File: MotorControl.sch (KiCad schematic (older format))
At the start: 6 parts, among them U3 74LVC125, X1 16MHz

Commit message: Add missing files from the TMC2130 branch.
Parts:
- C3, C81, C82, C90: footprint Capacitor_SMD:C_0603_1608Metric -> PrntrBoardV1:C_0603_1608Metric
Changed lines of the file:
@@
 F 0 "C3" H 8215 4346 50  0000 L CNN
 F 1 "0.1uF" H 8215 4255 50  0000 L CNN
-F 2 "Capacitor_SMD:C_0603_1608Metric" H 8138 4150 50  0001 C CNN
+F 2 "PrntrBoardV1:C_0603_1608Metric" H 8138 4150 50  0001 C CNN
 F 3 "~" H 8100 4300 50  0001 C CNN
 	1    8100 4300
@@
 F 0 "C90" H 9550 4350 50  0000 L CNN
 F 1 "0.1uF" H 9550 4250 50  0000 L CNN
-F 2 "Capacitor_SMD:C_0603_1608Metric" H 9488 4300 50  0001 C CNN
+F 2 "PrntrBoardV1:C_0603_1608Metric" H 9488 4300 50  0001 C CNN
 F 3 "~" H 9450 4450 50  0001 C CNN
 	1    9450 4450
@@
 F 0 "C81" H 7865 4346 50  0000 L CNN
 F 1 "1000pF" H 7800 4200 50  0000 L CNN
-F 2 "Capacitor_SMD:C_0603_1608Metric" H 7788 4150 50  0001 C CNN
+F 2 "PrntrBoardV1:C_0603_1608Metric" H 7788 4150 50  0001 C CNN
 F 3 "~" H 7750 4300 50  0001 C CNN
 	1    7750 4300
@@
 F 0 "C82" H 9250 4350 50  0000 L CNN
 F 1 "1000pF" H 9150 4150 50  0000 L CNN
-F 2 "Capacitor_SMD:C_0603_1608Metric" H 9238 4300 50  0001 C CNN
+F 2 "PrntrBoardV1:C_0603_1608Metric" H 9238 4300 50  0001 C CNN
 F 3 "~" H 9200 4450 50  0001 C CNN
 	1    9200 4450

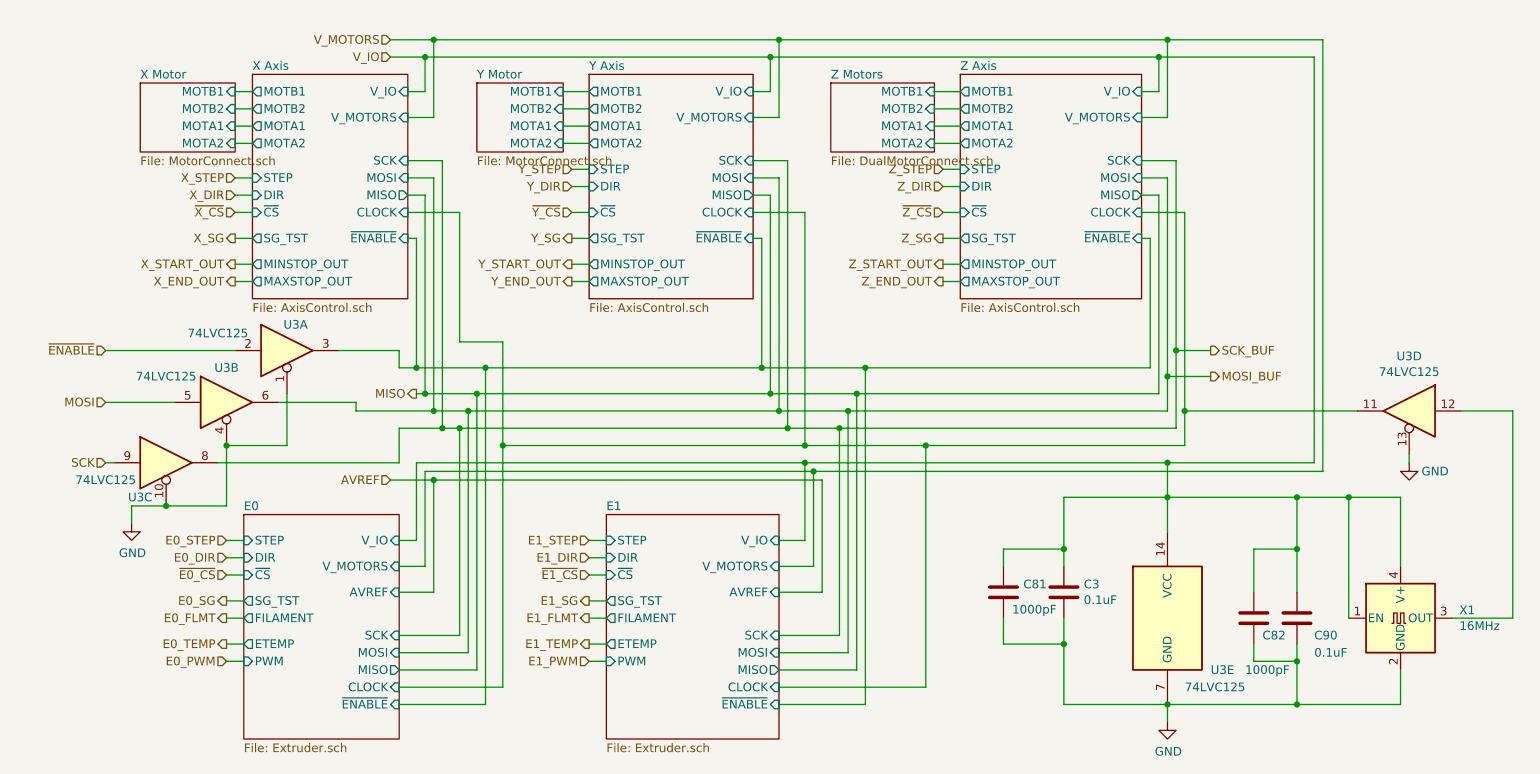
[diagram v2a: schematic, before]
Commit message: Update schematics to match rev3 of tmc2130 branch.
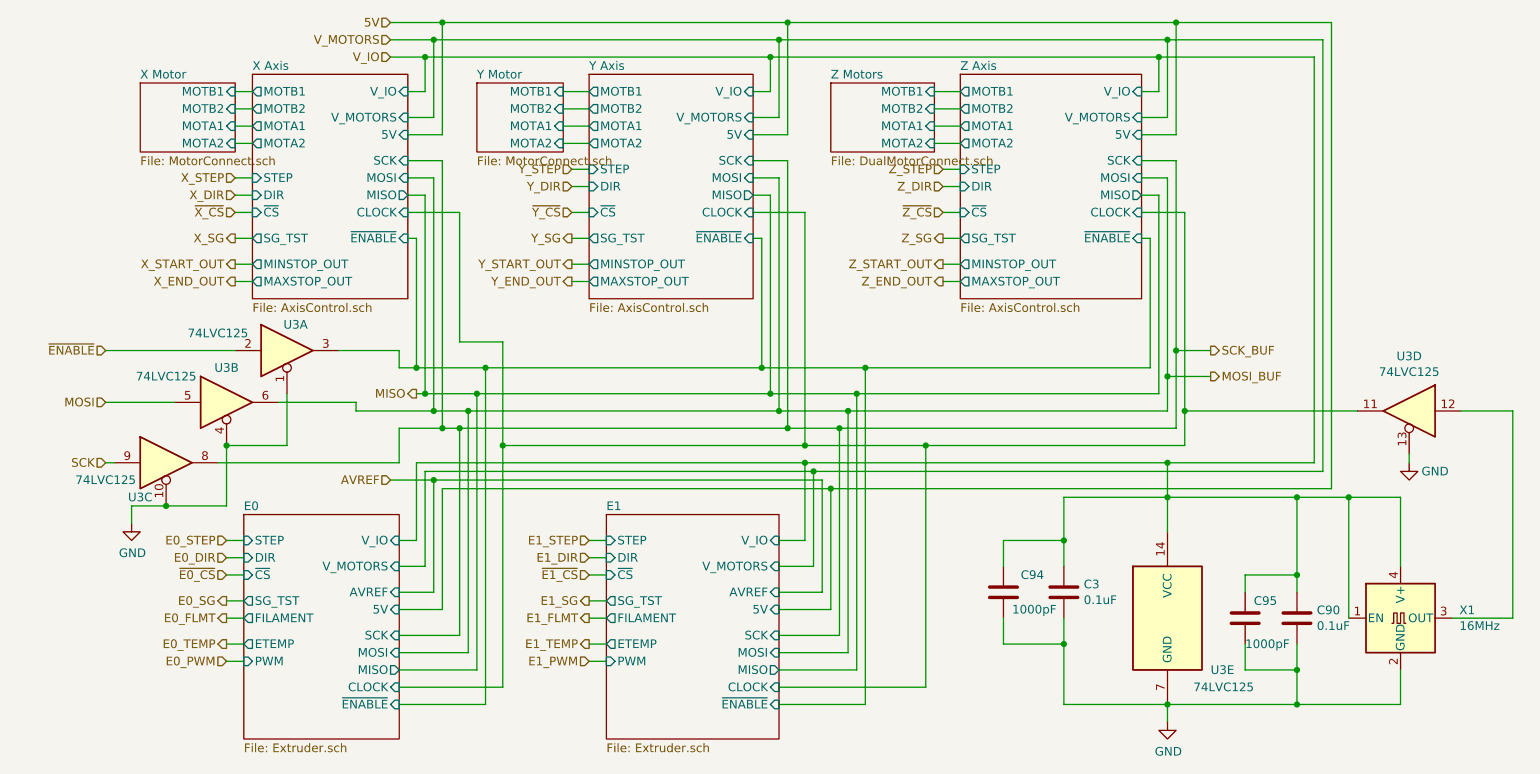
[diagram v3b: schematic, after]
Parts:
- removed C81, C82: 1000pF, PrntrBoardV1:C_0603_1608Metric, symbol Device:C
- added C94, C95: 1000pF, PrntrBoardV1:C_0603_1608Metric, symbol Device:C
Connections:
- net GND: now also C94.2, C95.2
- net V_IO: now also C94.1, C95.1
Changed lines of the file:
@@
 F14 "ETEMP" O L 3350 4600 50
 F15 "PWM" I L 3350 4700 50
-F16 "CLOCK" I R 4250 4850 50
+F16 "5V" I R 4250 4400 50
+F17 "CLOCK" I R 4250 4850 50
 $EndSheet
 $Sheet
@@
 F12 "MAXSTOP_OUT" O L 3400 2500 50
 F13 "MINSTOP_OUT" O L 3400 2400 50
-F14 "CLOCK" I R 4300 2100 50
-F15 "MOTA1" O L 3400 1600 50
-F16 "MOTB1" O L 3400 1400 50
-F17 "MOTA2" O L 3400 1700 50
-F18 "MOTB2" O L 3400 1500 50
+F14 "5V" I R 4300 1650 50
+F15 "CLOCK" I R 4300 2100 50
+F16 "MOTA1" O L 3400 1600 50
+F17 "MOTB1" O L 3400 1400 50
+F18 "MOTA2" O L 3400 1700 50
+F19 "MOTB2" O L 3400 1500 50
 $EndSheet
 $Sheet
@@
 F12 "MAXSTOP_OUT" O L 5350 2500 50
 F13 "MINSTOP_OUT" O L 5350 2400 50
-F14 "CLOCK" I R 6300 2100 50
-F15 "MOTA1" O L 5350 1600 50
-F16 "MOTB1" O L 5350 1400 50
-F17 "MOTA2" O L 5350 1700 50
-F18 "MOTB2" O L 5350 1500 50
+F14 "5V" I R 6300 1650 50
+F15 "CLOCK" I R 6300 2100 50
+F16 "MOTA1" O L 5350 1600 50
+F17 "MOTB1" O L 5350 1400 50
+F18 "MOTA2" O L 5350 1700 50
+F19 "MOTB2" O L 5350 1500 50
 $EndSheet
 Wire Wire Line
@@
 F12 "MAXSTOP_OUT" O L 7500 2500 50
 F13 "MINSTOP_OUT" O L 7500 2400 50
-F14 "CLOCK" I R 8550 2100 50
-F15 "MOTA1" O L 7500 1600 50
-F16 "MOTB1" O L 7500 1400 50
-F17 "MOTA2" O L 7500 1700 50
-F18 "MOTB2" O L 7500 1500 50
+F14 "5V" I R 8550 1650 50
+F15 "CLOCK" I R 8550 2100 50
+F16 "MOTA1" O L 7500 1600 50
+F17 "MOTB1" O L 7500 1400 50
+F18 "MOTA2" O L 7500 1700 50
+F19 "MOTB2" O L 7500 1500 50
 $EndSheet
 Wire Wire Line
@@
 F14 "ETEMP" O L 5450 4600 50
 F15 "PWM" I L 5450 4700 50
-F16 "CLOCK" I R 6450 4850 50
+F16 "5V" I R 6450 4400 50
+F17 "CLOCK" I R 6450 4850 50
 $EndSheet
 Wire Wire Line
@@
 Wire Wire Line
 	8700 3750 8700 3550
+Text HLabel 4200 1000 0    50   Input ~ 0
+5V
 Wire Wire Line
 	8700 3950 8700 3750
 Wire Wire Line
-	8100 4150 8100 4050
+	8100 4150 8100 4000
 Connection ~ 6950 3000
 Connection ~ 6900 3150
@@
 P 8700 4450
 F 0 "U3" H 8950 4150 50  0000 L CNN
-F 1 "74LVC125" H 8800 4050 50  0000 L CNN
+F 1 "74LVC125" H 8850 4050 50  0000 L CNN
 F 2 "Package_SO:TSSOP-14_4.4x5mm_P0.65mm" H 8700 4450 50  0001 C CNN
 F 3 "http://www.ti.com/lit/gpn/sn74LVC125" H 8700 4450 50  0001 C CNN
@@
 	4450 3650 4450 4300
 Wire Wire Line
+	4200 1000 4500 1000
+Wire Wire Line
+	9650 1000 9650 3700
+Wire Wire Line
+	9650 3700 6750 3700
+Wire Wire Line
+	4500 3700 4500 4400
+Wire Wire Line
+	4500 4400 4250 4400
+Wire Wire Line
+	6450 4400 6750 4400
+Wire Wire Line
+	6750 4400 6750 3700
+Connection ~ 6750 3700
+Wire Wire Line
+	6750 3700 4500 3700
+Wire Wire Line
+	8550 1650 8750 1650
+Wire Wire Line
+	8750 1650 8750 1000
+Connection ~ 8750 1000
+Wire Wire Line
+	8750 1000 9650 1000
+Wire Wire Line
+	6300 1650 6500 1650
+Wire Wire Line
+	6500 1650 6500 1000
+Connection ~ 6500 1000
+Wire Wire Line
+	6500 1000 8750 1000
+Wire Wire Line
+	4300 1650 4500 1650
+Wire Wire Line
+	4500 1650 4500 1000
+Connection ~ 4500 1000
+Wire Wire Line
+	4500 1000 6500 1000
+Wire Wire Line
 	4350 3150 4400 3150
 Connection ~ 4400 3150
@@
 Wire Wire Line
 	7300 3450 6600 3450
+Wire Wire Line
+	8800 2100 8800 3250
+Wire Wire Line
+	8800 3250 9800 3250
+Connection ~ 8800 3250
+Wire Wire Line
+	8800 3250 8800 3450
 $Comp
 L Oscillator:XO32 X1
@@
 U 1 1 5AFD7ED2
 P 9450 4450
-F 0 "C90" H 9550 4350 50  0000 L CNN
-F 1 "0.1uF" H 9550 4250 50  0000 L CNN
+F 0 "C90" H 9565 4496 50  0000 L CNN
+F 1 "0.1uF" H 9565 4405 50  0000 L CNN
 F 2 "PrntrBoardV1:C_0603_1608Metric" H 9488 4300 50  0001 C CNN
 F 3 "~" H 9450 4450 50  0001 C CNN
@@
 	9750 3750 10050 3750
 Wire Wire Line
-	9450 4300 9450 4050
+	9450 4300 9450 4200
 Connection ~ 9450 3750
 Wire Wire Line
 	9450 3750 9750 3750
 Wire Wire Line
-	9450 4600 9450 4700
+	9450 4600 9450 4750
 Connection ~ 9450 4950
 Wire Wire Line
@@
 Wire Wire Line
 	8750 2900 8750 1800
-Wire Wire Line
-	8800 2100 8800 3250
-Wire Wire Line
-	9800 3250 8800 3250
-Connection ~ 8800 3250
-Wire Wire Line
-	8800 3250 8800 3450
-$Comp
-L Device:C C81
-U 1 1 5B400CE8
+$Comp
+L Device:C C94
+U 1 1 5B3B1C87
 P 7750 4300
-F 0 "C81" H 7865 4346 50  0000 L CNN
+F 0 "C94" H 7850 4400 50  0000 L CNN
 F 1 "1000pF" H 7800 4200 50  0000 L CNN
 F 2 "PrntrBoardV1:C_0603_1608Metric" H 7788 4150 50  0001 C CNN
@@
 $EndComp
 $Comp
-L Device:C C82
-U 1 1 5B400D4B
-P 9200 4450
-F 0 "C82" H 9250 4350 50  0000 L CNN
-F 1 "1000pF" H 9150 4150 50  0000 L CNN
-F 2 "PrntrBoardV1:C_0603_1608Metric" H 9238 4300 50  0001 C CNN
-F 3 "~" H 9200 4450 50  0001 C CNN
-	1    9200 4450
-	1    0    0    -1
-$EndComp
-Wire Wire Line
-	9200 4300 9200 4050
-Wire Wire Line
-	9200 4050 9450 4050
-Connection ~ 9450 4050
-Wire Wire Line
-	9450 4050 9450 3750
-Wire Wire Line
-	9200 4600 9200 4700
-Wire Wire Line
-	9200 4700 9450 4700
-Connection ~ 9450 4700
-Wire Wire Line
-	9450 4700 9450 4950
-Wire Wire Line
-	7750 4150 7750 4050
-Wire Wire Line
-	7750 4050 8100 4050
-Connection ~ 8100 4050
-Wire Wire Line
-	8100 4050 8100 3750
+L Device:C C95
+U 1 1 5B3B1D02
+P 9150 4450
+F 0 "C95" H 9200 4550 50  0000 L CNN
+F 1 "1000pF" H 9150 4300 50  0000 L CNN
+F 2 "PrntrBoardV1:C_0603_1608Metric" H 9188 4300 50  0001 C CNN
+F 3 "~" H 9150 4450 50  0001 C CNN
+	1    9150 4450
+	1    0    0    -1
+$EndComp
+Wire Wire Line
+	9150 4600 9150 4750
+Wire Wire Line
+	9150 4750 9450 4750
+Connection ~ 9450 4750
+Wire Wire Line
+	9450 4750 9450 4950
+Wire Wire Line
+	9150 4300 9150 4200
+Wire Wire Line
+	9150 4200 9450 4200
+Connection ~ 9450 4200
+Wire Wire Line
+	9450 4200 9450 3750
+Wire Wire Line
+	7750 4150 7750 4000
+Wire Wire Line
+	7750 4000 8100 4000
+Connection ~ 8100 4000
+Wire Wire Line
+	8100 4000 8100 3750
 Wire Wire Line
 	7750 4450 7750 4600

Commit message: Reset schematics for tmc2660. Clean the board layout.
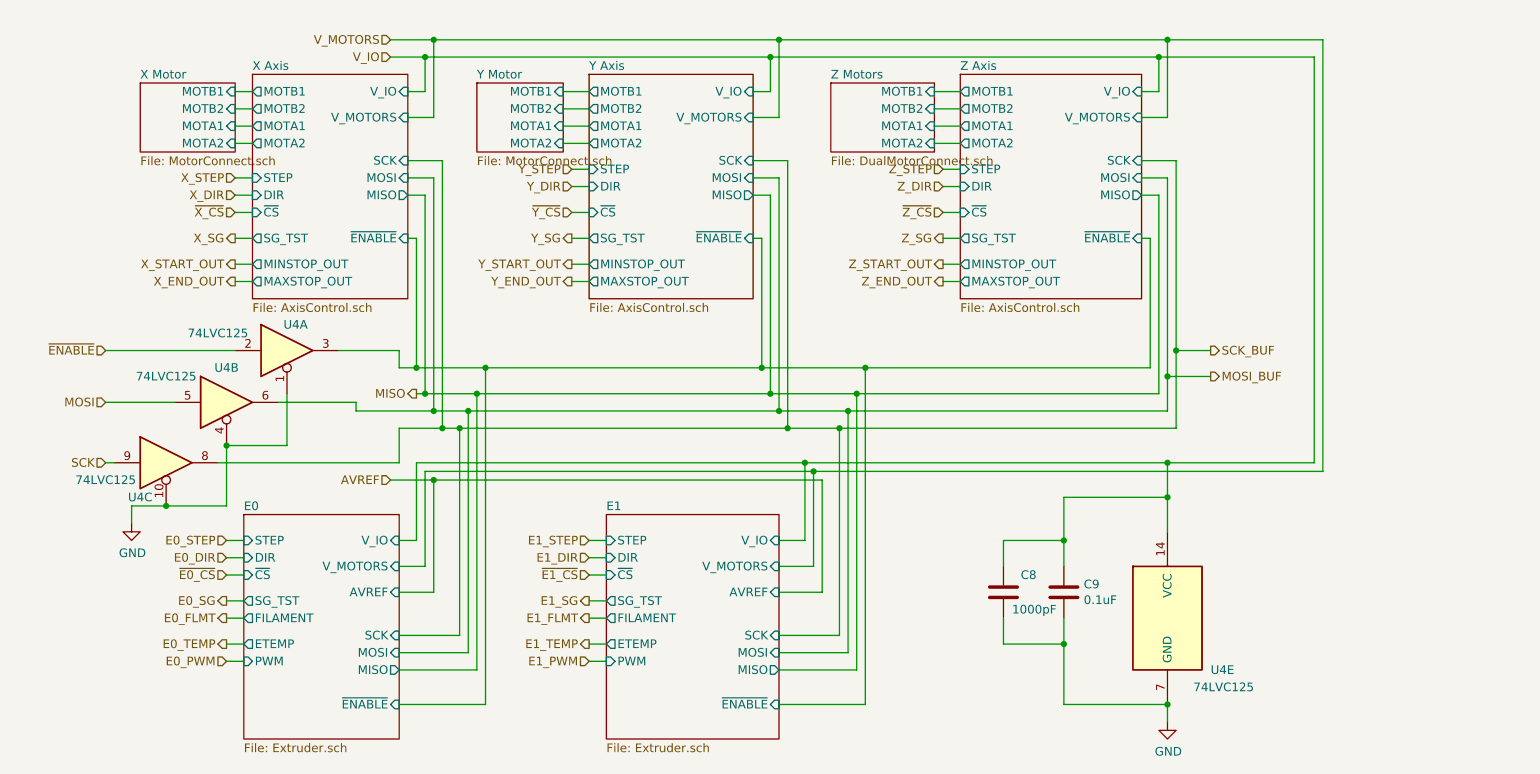
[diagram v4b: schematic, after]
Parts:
- removed C90: 0.1uF, PrntrBoardV1:C_0603_1608Metric, symbol Device:C
- removed C95: 1000pF, PrntrBoardV1:C_0603_1608Metric, symbol Device:C
- removed unit 4 of U3
- removed X1: 16MHz, PrntrBoardV1:Oscillator_SMD_EuroQuartz_XO32-4Pin_3.2x2.5mm_HandSoldering, symbol Oscillator:XO32
- renumbered C94 to C8, C3 to C9, U3 to U4

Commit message: Completed. Added labels, small tweaks. Ready for fabrication.
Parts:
- added unit 4 of U4
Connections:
- net GND: now also U4.12
- net V_IO: now also U4.13
- no-connect marks 0 -> 1
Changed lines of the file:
@@
 F15 "PWM" I L 5450 4700 50
 $EndSheet
+$Comp
+L 74ls125:74LVC125 U4
+U 4 1 5C47A3BD
+P 9550 4450
+F 0 "U4" H 9550 4675 50  0000 C CNN
+F 1 "74LVC125" H 9550 4766 50  0000 C CNN
+F 2 "" H 9550 4450 50  0001 C CNN
+F 3 "http://www.ti.com/lit/gpn/sn74LVC125" H 9550 4450 50  0001 C CNN
+	4    9550 4450
+	-1   0    0    1
+$EndComp
+Wire Wire Line
+	9850 4450 9850 4950
+Wire Wire Line
+	9850 4950 8700 4950
+Wire Wire Line
+	9550 4200 9550 3750
+Wire Wire Line
+	9550 3750 8700 3750
+NoConn ~ 9250 4450
 $EndSCHEMATC

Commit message: Updated component values, updated component footprint.
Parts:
- U4: footprint (none) -> Package_SO:TSSOP-14_4.4x5mm_P0.65mm
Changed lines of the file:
@@
 F 0 "U4" H 9550 4675 50  0000 C CNN
 F 1 "74LVC125" H 9550 4766 50  0000 C CNN
-F 2 "" H 9550 4450 50  0001 C CNN
+F 2 "Package_SO:TSSOP-14_4.4x5mm_P0.65mm" H 9550 4450 50  0001 C CNN
 F 3 "http://www.ti.com/lit/gpn/sn74LVC125" H 9550 4450 50  0001 C CNN
 	4    9550 4450
